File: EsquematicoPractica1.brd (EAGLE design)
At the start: 100 x 80 mm, 129 parts, among them IC1 GSOT05C-GS08, IC10 NCP1117ST33T3G, IC2 RCV420JP, IC3 TC7662BEOA, IC4 MC7812BTG, IC5 RCV420JP, IC6 TC7662BEOA, IC7 MC7812BTG, IC8 GSOT05C-GS08, J2 M50-3500542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

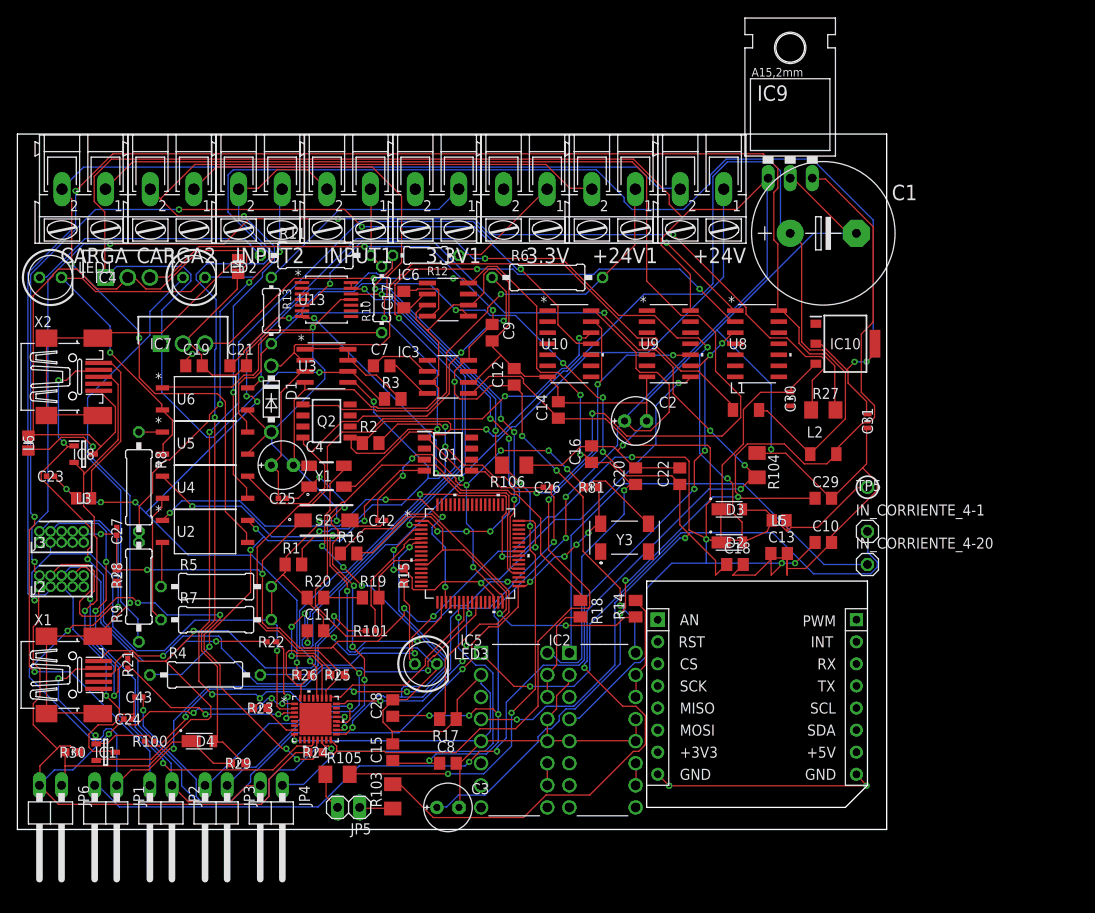
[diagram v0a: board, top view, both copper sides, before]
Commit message: Practica 1 - Total Entrega
PCB + Esquematico
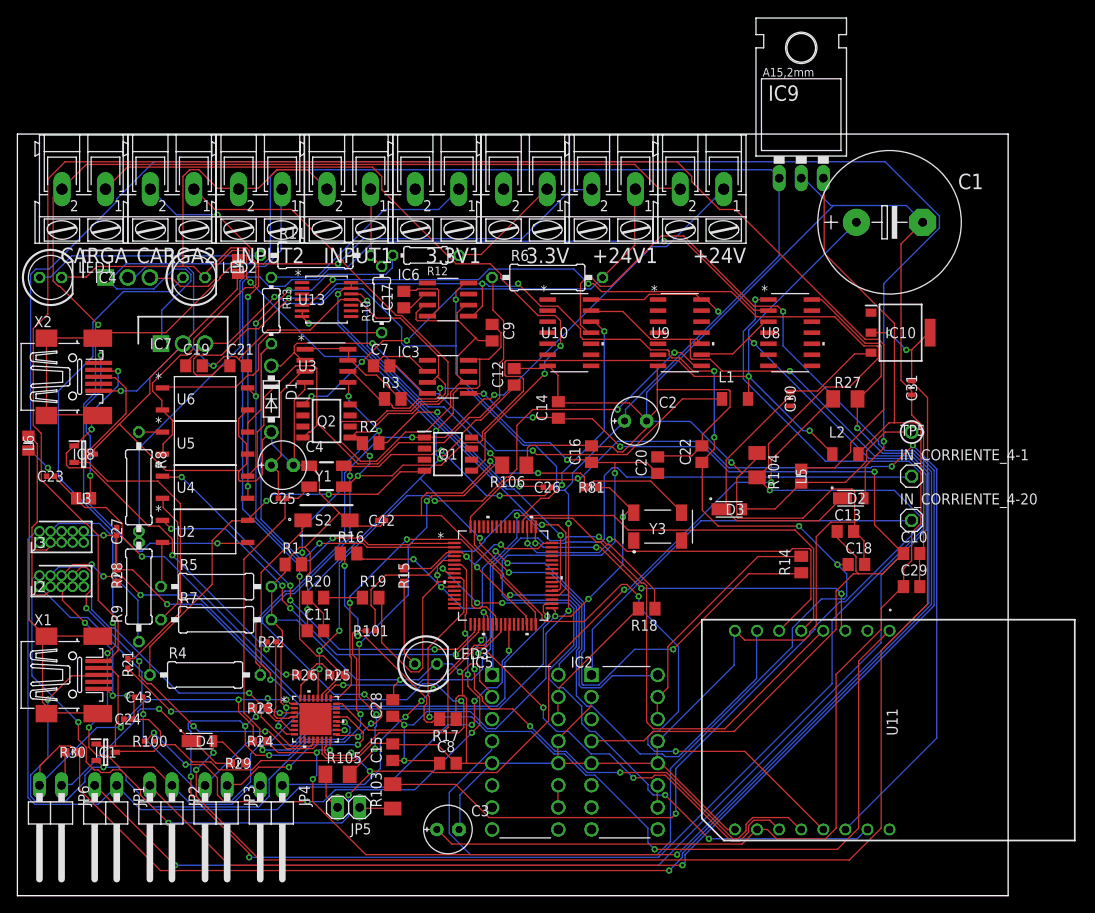
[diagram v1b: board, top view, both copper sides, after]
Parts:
- removed U$1: MIKROE_CLICKMINI, mikrobus_lib:MIKROE_BUS_MINI
- added U11: MIKROE-971, MIKROE-971:MIKROE-971_1
- moved R14 19.7 mm to (90.2, 30.5)
- moved D2 14.9 mm to (96.5, 38.1)
- moved C29 14.4 mm to (102.9, 27.9)
- moved C18 14.0 mm to (96.5, 30.5)
- moved C10 10.2 mm to (102.9, 31.8)
- moved IN_CORRIENTE_4-1 8.13 mm to (102.9, 40.6)
- moved TP5 8.13 mm to (102.9, 45.7)
- moved C13 8.03 mm to (95.2, 34.3)
- moved C1 7.73 mm to (100.3, 69.8)
- moved R18 7.62 mm to (72.4, 25.4), turned to 180 degrees
- moved IN_CORRIENTE_4-20 7.18 mm to (102.9, 35.6)
- moved R24 6.48 mm to (27.9, 10.2)
- moved IC10 6.48 mm to (101.6, 57.1)
- moved C31 6.35 mm to (102.9, 50.8)
- moved L5 5.68 mm to (90.2, 40.6), turned to 270 degrees
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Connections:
- net +3V3: now also U11.7; no longer U$1.P$7
- net +5V: now also U11.10; no longer U$1.P$10
- net GND: now also U11.8, U11.9; no longer U$1.P$8, U$1.P$9
- net I2C0_SCL: now also U11.12; no longer U$1.P$12
- net I2C0_SDA: now also U11.11; no longer U$1.P$11
- net LPUART0_RX_MKB: now also U11.13; no longer U$1.P$14
- net LPUART0_TX_MKB: now also U11.14; no longer U$1.P$13
- net PIN_INT: now also U11.15; no longer U$1.P$15
- net PTA20_RST: now also U11.2; no longer U$1.P$2
- net PTE20_A0: now also U11.1; no longer U$1.P$1
- net SPI0_MISO: now also U11.5; no longer U$1.P$5
- net SPI0_MOSI: now also U11.6; no longer U$1.P$6
- net SPI0_PCS0: now also U11.3; no longer U$1.P$3
- net SPI0_SCK: now also U11.4; no longer U$1.P$4
- net TPM0_CH2_PWM: no longer U$1.P$16
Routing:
- net LPUART0_TX_MKB: track 0.00 -> 107.7 mm, vias 0 -> 3
- net PTE20_A0: track 0.00 -> 100.6 mm, vias 0 -> 2
- net N$72: track 103.8 -> 188.3 mm, vias 4 -> 0
- net GND: track 634.4 -> 718.6 mm, vias 11 -> 10
- net N$40: track 121.7 -> 197.6 mm
- net PIN_INT: track 0.00 -> 74.1 mm, vias 0 -> 5
- net LPUART0_RX_MKB: track 0.00 -> 72.4 mm, vias 0 -> 2
- net SDA_SWD_EN: track 94.0 -> 164.6 mm, vias 3 -> 5
- net SPI0_SCK: track 0.00 -> 58.4 mm
- net I2C0_SCL: track 0.00 -> 55.0 mm, vias 0 -> 4
- net N$6: track 138.1 -> 83.6 mm
- net SDA_P20: track 132.0 -> 186.5 mm, vias 5 -> 7
- net P5V_SDA: track 157.7 -> 211.6 mm, vias 9 -> 4
- net I2C0_SDA: track 0.00 -> 53.3 mm, vias 0 -> 4
- net N$58: track 114.8 -> 162.6 mm, vias 6 -> 2
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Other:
- board size 100 x 80 mm -> 114 x 87.6 mm

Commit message: Práctica 1 - Entregada y Corregida
Con todos sus valores adecuados, esquematico y PCB, solo faltó ROUTEAR adecuadamente con criterios como estabilidad en las fuentes y demas.
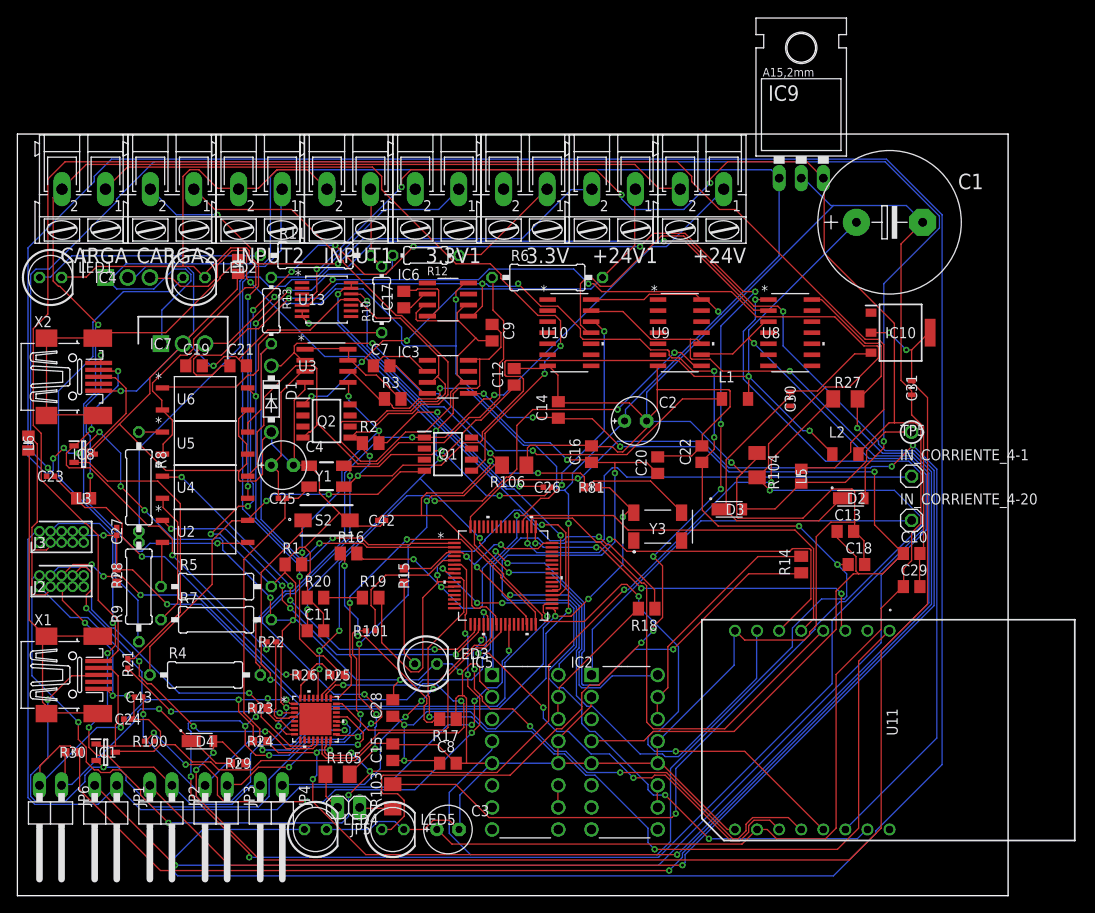
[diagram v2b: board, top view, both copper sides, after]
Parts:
- added LED4, LED5: (no value), led:LED5MM
- R11, R9: value 130 -> 1k
- R5, R7: value 10K -> 1K
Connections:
- removed net VDD: U13.4
- new net N$59: LED4.A, R7.2
- new net N$60: LED5.A, R5.2
- net +5V: now also U13.4
- net GND: now also LED4.K, LED5.K; no longer R5.2, R7.2
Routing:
- net N$59: track 0.00 -> 357.4 mm, vias 0 -> 7
- net N$60: track 0.00 -> 199.1 mm, vias 0 -> 13
- net +5V: track 138.8 -> 212.5 mm, vias 0 -> 4
- net GND: track 718.6 -> 737.5 mm, vias 10 -> 11
